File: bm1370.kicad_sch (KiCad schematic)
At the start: 49 parts, among them U5 MCP1824T-1202E/OT, U6 MCP1824T-0802E, U7 25MHz, U8 BM1370_mode1, U9 SN74AVC4T774

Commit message: added alternate part number for the 25MHz ASIC oscillator
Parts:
- U7: ME (none) -> 449-LFSPXO076024CUTT
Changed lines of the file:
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@@
+			)
+		)
+		(property "ME" "449-LFSPXO076024CUTT"
+			(at 41.91 171.45 0)
+			(effects
+				(font
+					(size 1.27 1.27)
+				)
+				(hide yes)
 			)
 		)

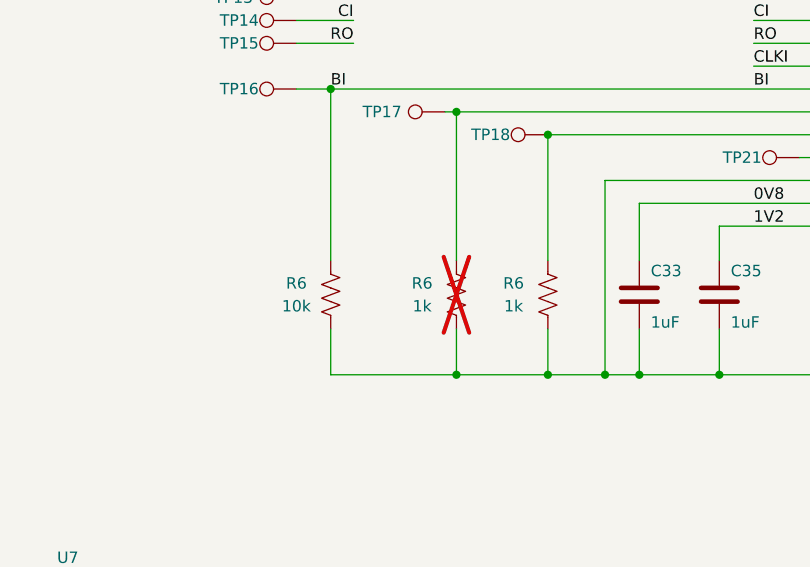
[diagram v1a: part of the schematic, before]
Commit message: update to KiCad v9
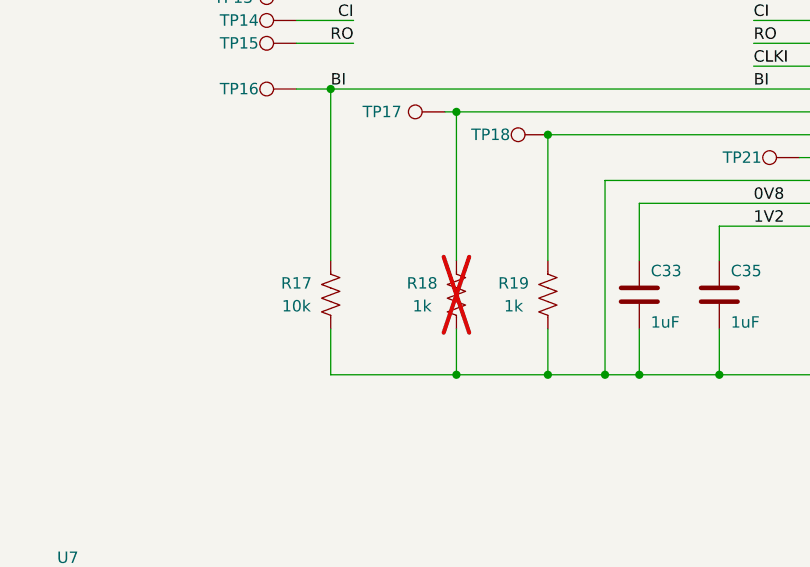
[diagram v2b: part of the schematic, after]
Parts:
- renumbered R6 to R17, R6 to R18, R6 to R19
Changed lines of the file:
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@@
 (kicad_sch
-	(version 20231120)
+	(version 20250114)
 	(generator "eeschema")
-	(generator_version "8.0")
+	(generator_version "9.0")
 	(paper "A")
 	(title_block
@@
 		(rev "601")
 	)
+	(text "Reference Voltage Regulators"
+		(exclude_from_sim no)
+		(at 38.1 22.86 0)
+		(effects
+			(font
+				(size 1.27 1.27)
+			)
+			(justify left bottom)
+		)
+	)
+	(text "Direction Control\nHIGH= A -> B\nLOW = A <- B"
+		(exclude_from_sim no)
+		(at 205.74 66.04 0)
+		(effects
+			(font
+				(size 1.27 1.27)
+			)
+			(justify left bottom)
+		)
+	)
 	(junction
 		(at 180.34 146.05)
@@
 		)
 	)
-	(text "Reference Voltage Regulators"
-		(exclude_from_sim no)
-		(at 38.1 22.86 0)
-		(effects
-			(font
-				(size 1.27 1.27)
-			)
-			(justify left bottom)
-		)
-	)
-	(text "Direction Control\nHIGH= A -> B\nLOW = A <- B"
-		(exclude_from_sim no)
-		(at 205.74 66.04 0)
-		(effects
-			(font
-				(size 1.27 1.27)
-			)
-			(justify left bottom)
-		)
-	)
 	(label "GND"
 		(at 45.72 43.18 0)
-		(fields_autoplaced yes)
 		(effects
 			(font
@@
 	(label "RST_N"
 		(at 69.85 104.14 180)
-		(fields_autoplaced yes)
 		(effects
 			(font
@@
 	(label "GND"
 		(at 229.87 46.99 180)
-		(fields_autoplaced yes)
 		(effects
 			(font
@@
 	(label "1V2"
 		(at 114.3 129.54 0)
-		(fields_autoplaced yes)
 		(effects
 			(font
@@
 	(label "1V2"
 		(at 68.58 29.21 0)
-		(fields_autoplaced yes)
 		(effects
 			(font
@@
 	(label "BI"
 		(at 67.31 114.3 0)
-		(fields_autoplaced yes)
 		(effects
 			(font
@@
 	(label "GND"
 		(at 27.94 172.72 0)
-		(fields_autoplaced yes)
 		(effects
 			(font
@@
 	(label "CLKO"
 		(at 171.45 111.76 180)
-		(fields_autoplaced yes)
 		(effects
 			(font
@@
 	(label "RST_N"
 		(at 114.3 104.14 0)
-		(fields_autoplaced yes)
 		(effects
 			(font
@@
 	(label "5V"
 		(at 29.21 55.88 0)
-		(fields_autoplaced yes)
 		(effects
 			(font
@@
 	(label "RO"
 		(at 114.3 109.22 0)
-		(fields_autoplaced yes)
 		(effects
 			(font
@@
 	(label "0V8"
 		(at 69.85 55.88 0)
-		(fields_autoplaced yes)
 		(effects
 			(font
@@
 	(label "CO"
 		(at 215.9 106.68 0)
-		(fields_autoplaced yes)
 		(effects
 			(font
@@
 	(label "GND"
 		(at 144.78 146.05 0)
-		(fields_autoplaced yes)
 		(effects
 			(font
@@
 	(label "BO"
 		(at 215.9 114.3 0)
-		(fields_autoplaced yes)
 		(effects
 			(font
@@
 	(label "GND"
 		(at 198.12 40.64 0)
-		(fields_autoplaced yes)
 		(effects
 			(font
@@
 	(label "5V"
 		(at 27.94 29.21 0)
-		(fields_autoplaced yes)
 		(effects
 			(font
@@
 	(label "CI"
 		(at 198.12 35.56 0)
-		(fields_autoplaced yes)
 		(effects
 			(font
@@
 	(label "GND"
 		(at 229.87 52.07 180)
-		(fields_autoplaced yes)
 		(effects
 			(font
@@
 	(label "PIN_MODE"
 		(at 215.9 121.92 0)
-		(fields_autoplaced yes)
 		(effects
 			(font
@@
 	(label "1V2"
 		(at 229.87 49.53 180)
-		(fields_autoplaced yes)
 		(effects
 			(font
@@
 	(label "CI"
 		(at 69.85 106.68 180)
-		(fields_autoplaced yes)
 		(effects
 			(font
@@
 	(label "1V2"
 		(at 27.94 170.18 0)
-		(fields_autoplaced yes)
 		(effects
 			(font
@@
 	(label "RO"
 		(at 198.12 38.1 0)
-		(fields_autoplaced yes)
 		(effects
 			(font
@@
 	(label "NRSTO"
 		(at 215.9 104.14 0)
-		(fields_autoplaced yes)
 		(effects
 			(font
@@
 	(label "PIN_MODE"
 		(at 171.45 121.92 180)
-		(fields_autoplaced yes)
 		(effects
 			(font
@@
 	(label "0V8"
 		(at 114.3 127 0)
-		(fields_autoplaced yes)
 		(effects
 			(font
@@
 	(label "GND"
 		(at 46.99 69.85 0)
-		(fields_autoplaced yes)
 		(effects
 			(font
@@
 	(label "VDD3_1"
 		(at 171.45 99.06 180)
-		(fields_autoplaced yes)
 		(effects
 			(font
@@
 	(label "VDD2_1"
 		(at 171.45 96.52 180)
-		(fields_autoplaced yes)
 		(effects
 			(font
@@
 	(label "RI"
 		(at 215.9 109.22 0)
-		(fields_autoplaced yes)
 		(effects
 			(font
@@
 	(label "RST_N"
 		(at 198.12 33.02 0)
-		(fields_autoplaced yes)
 		(effects
 			(font
@@
 	(label "CLKI"
 		(at 114.3 111.76 0)
-		(fields_autoplaced yes)
 		(effects
 			(font
@@
 	(label "1V2"
 		(at 198.12 29.21 0)
-		(fields_autoplaced yes)
 		(effects
 			(font
@@
 	(label "CO"
 		(at 171.45 106.68 180)
-		(fields_autoplaced yes)
 		(effects
 			(font
@@
 	(label "VDD1_0"
 		(at 114.3 93.98 0)
-		(fields_autoplaced yes)
 		(effects
 			(font
@@
 	(label "VDD3_0"
 		(at 114.3 99.06 0)
-		(fields_autoplaced yes)
 		(effects
 			(font
@@
 	(label "CLKO"
 		(at 215.9 111.76 0)
-		(fields_autoplaced yes)
 		(effects
 			(font
@@
 	(label "CLKI"
 		(at 57.15 170.18 180)
-		(fields_autoplaced yes)
 		(effects
 			(font
@@
 	(label "3V3"
 		(at 231.14 29.21 0)
-		(fields_autoplaced yes)
 		(effects
 			(font
@@
 	(label "RO"
 		(at 69.85 109.22 180)
-		(fields_autoplaced yes)
 		(effects
 			(font
@@
 	(label "VDD1_1"
 		(at 171.45 93.98 180)
-		(fields_autoplaced yes)
 		(effects
 			(font
@@
 	(label "GND"
 		(at 81.28 101.6 0)
-		(fields_autoplaced yes)
 		(effects
 			(font
@@
 	(label "VDD"
 		(at 143.51 85.09 0)
-		(fields_autoplaced yes)
 		(effects
 			(font
@@
 	(label "BO"
 		(at 171.45 114.3 180)
-		(fields_autoplaced yes)
 		(effects
 			(font
@@
 	(label "GND"
 		(at 215.9 59.69 180)
-		(fields_autoplaced yes)
 		(effects
 			(font
@@
 	(label "RI"
 		(at 171.45 109.22 180)
-		(fields_autoplaced yes)
 		(effects
 			(font
@@
 	(label "1V2"
 		(at 57.15 172.72 180)
-		(fields_autoplaced yes)
 		(effects
 			(font
@@
 	(label "VDD2_0"
 		(at 114.3 96.52 0)
-		(fields_autoplaced yes)
 		(effects
 			(font
@@
 	(label "NRSTO"
 		(at 171.45 104.14 180)
-		(fields_autoplaced yes)
 		(effects
 			(font
@@
 	(label "GND"
 		(at 200.66 101.6 0)
-		(fields_autoplaced yes)
 		(effects
 			(font
@@
 	(label "GND"
 		(at 133.35 63.5 180)
-		(fields_autoplaced yes)
 		(effects
 			(font
@@
 	(label "GND"
 		(at 229.87 44.45 180)
-		(fields_autoplaced yes)
 		(effects
 			(font
@@
 	(label "CI"
 		(at 114.3 106.68 0)
-		(fields_autoplaced yes)
 		(effects
 			(font
@@
 	(label "VDD"
 		(at 128.27 50.8 0)
-		(fields_autoplaced yes)
 		(effects
 			(font
@@
 	(label "BI"
 		(at 114.3 114.3 0)
-		(fields_autoplaced yes)
 		(effects
 			(font
@@
 		(shape input)
 		(at 27.94 29.21 180)
-		(fields_autoplaced yes)
 		(effects
 			(font
@@
 		(shape output)
 		(at 176.53 116.84 0)
-		(fields_autoplaced yes)
 		(effects
 			(font
@@
 		(shape input)
 		(at 242.57 29.21 0)
-		(fields_autoplaced yes)
 		(effects
 			(font
@@
 		(shape input)
 		(at 229.87 35.56 0)
-		(fields_autoplaced yes)
 		(effects
 			(font
@@
 		(shape output)
 		(at 229.87 38.1 0)
-		(fields_autoplaced yes)
 		(effects
 			(font
@@
 		(shape input)
 		(at 134.62 81.28 180)
-		(fields_autoplaced yes)
 		(effects
 			(font
@@
 		(shape input)
 		(at 229.87 33.02 0)
-		(fields_autoplaced yes)
 		(effects
 			(font
@@
 		(shape output)
 		(at 176.53 119.38 0)
-		(fields_autoplaced yes)
 		(effects
 			(font
@@
 		(on_board yes)
 		(dnp yes)
-		(property "Reference" "R6"
+		(property "Reference" "R18"
 			(at 77.47 135.89 0)
 			(effects
@@
 		(on_board yes)
 		(dnp no)
-		(property "Reference" "R6"
+		(property "Reference" "R19"
 			(at 87.63 135.89 0)
 			(effects
@@
 		(on_board yes)
 		(dnp no)
-		(property "Reference" "R6"
+		(property "Reference" "R17"
 			(at 63.5 135.89 0)
 			(effects
